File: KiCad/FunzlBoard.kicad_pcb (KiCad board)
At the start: 2 copper layers, 174 x 149 mm, 151 parts, among them J1 Poti, J10 Slider, J11 Toggle, J12 Button Small, J13 Virb.1, J14 Vibr.2, J15 5V IN, J16 BAT, J17 LED G, J18 LED R, J19 PWR Switch, J2 Banana Plug Socket 1, J20 BAT Monitor, J21 LED Blink, J22 BZ 1, J23 BZ 2, J24 BZ 3, J3 Banana Plug Socket 2, J4 Banana Plug Socket 3, J5 3-Way, J6 2-Way 1, J7 2-Way 2, J8 2-Way 3, J9 Rocker, Q1 2N7002, Q2 2N7002, SW1 Button R, SW2 Button Y, SW3 Button G, SW4 Button B, SW5 SW_MEC_5E, U1 ESP32-C3_SUPERMINI_SMD, U2 ADS7828, U3 MCP23017_SO

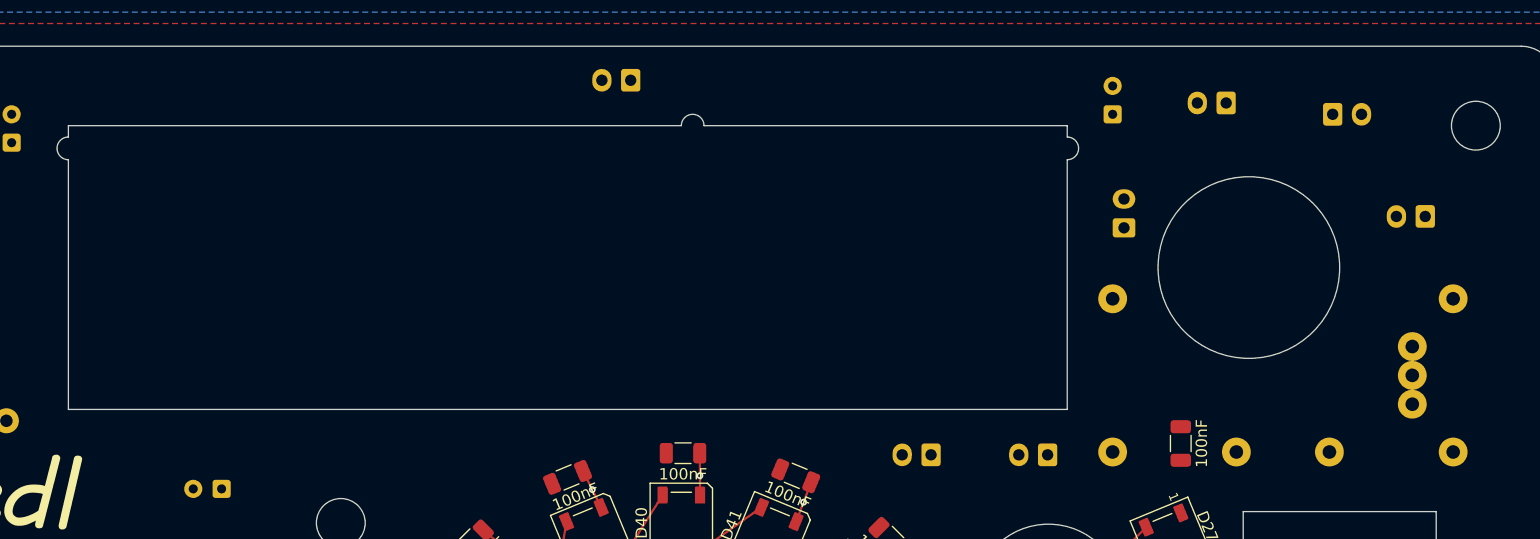
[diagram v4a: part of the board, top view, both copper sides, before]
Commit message: Add fuse
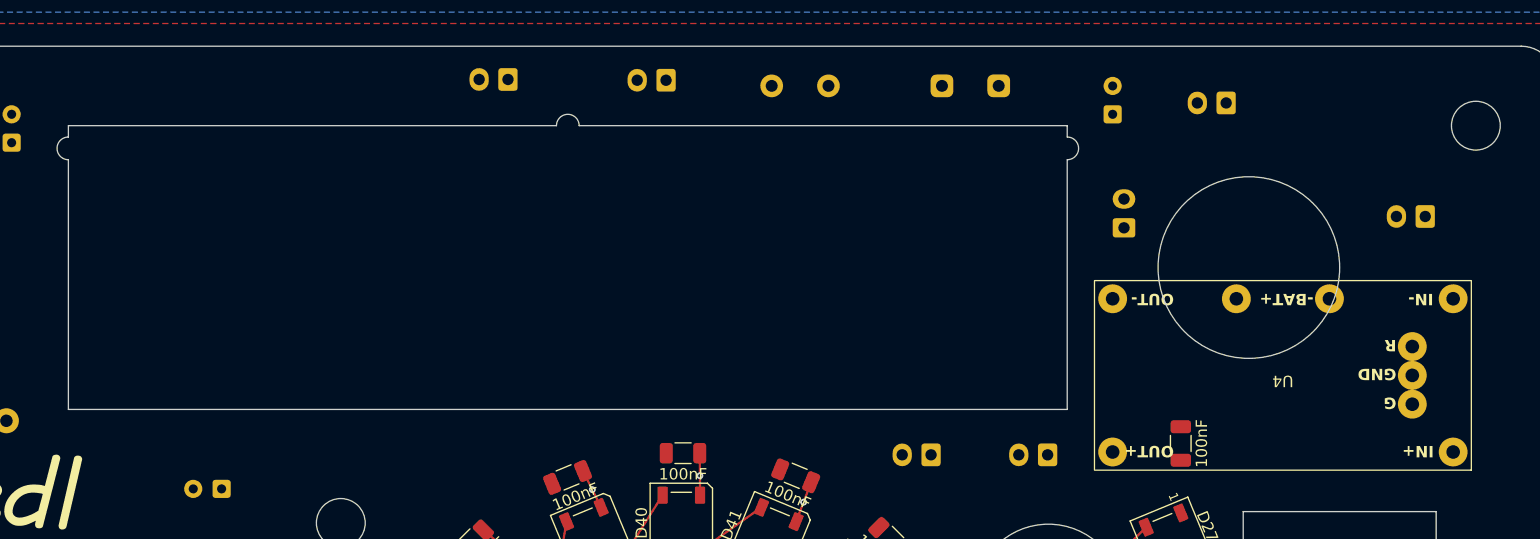
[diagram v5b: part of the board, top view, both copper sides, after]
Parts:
- added F1: Fuse, Fuse:Fuseholder_Clip-5x20mm_Littelfuse_111_Inline_P20.00x5.00mm_D1.05mm_Horizontal, B.Cu at (128.0, 6.49)
- U4: moved to F.Cu
- moved J16 61.3 mm to (97.4, 6.00), turned to 180 degrees
- moved J23 10.8 mm to (83.5, 5.93)
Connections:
- J20 pad 2: Net-(J16-Pin_1) -> Net-(J20-Pin_2)
- SW5 pad 1: Net-(J16-Pin_1) -> Net-(J20-Pin_2)
- SW5 pad 2: Net-(J16-Pin_1) -> Net-(J20-Pin_2)
- U4 pad 4: Net-(J16-Pin_1) -> Net-(J20-Pin_2)
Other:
- outline, holes or cut-outs redrawn
